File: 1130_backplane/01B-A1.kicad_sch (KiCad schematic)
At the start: 91 parts

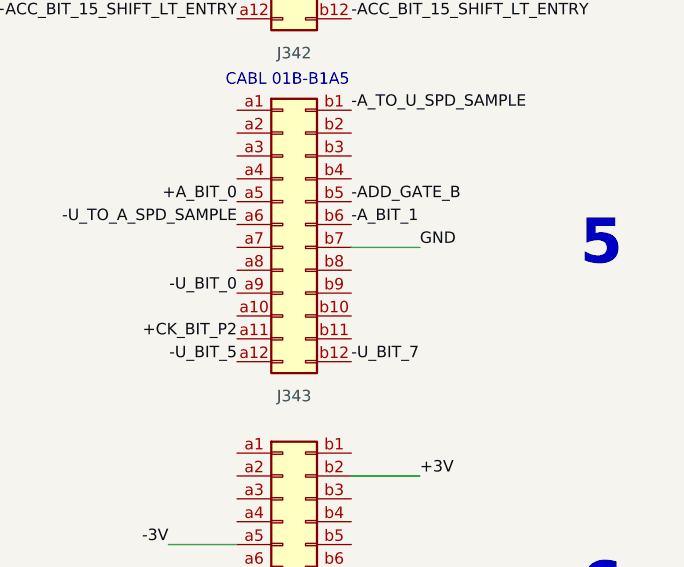
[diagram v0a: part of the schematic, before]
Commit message: Finish page RA201-RA271
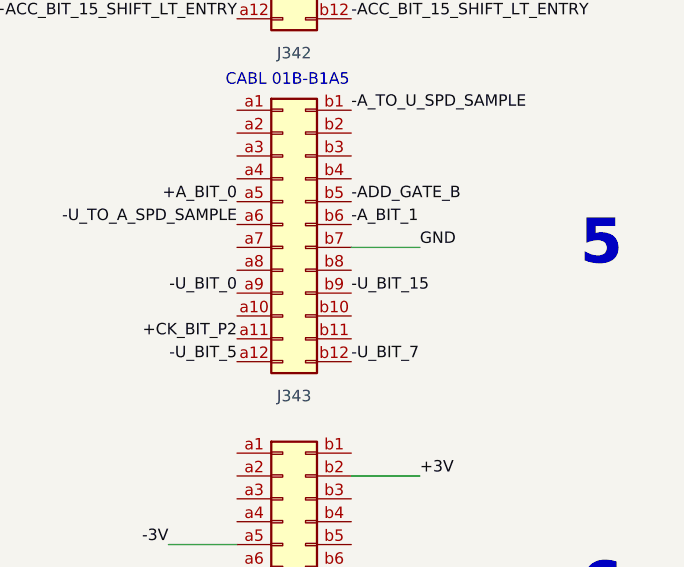
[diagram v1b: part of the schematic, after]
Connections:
- net -U_BIT_15: now also J342.b9 (Pin_b9)
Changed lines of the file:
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@@
     (effects (font (size 1.27 1.27)) (justify right bottom))
+  )
+  (label "-U_BIT_15" (at 807.72 238.76 0)
+    (effects (font (size 1.27 1.27)) (justify left bottom))
   )
   (label "-T3_SP" (at 477.52 236.22 180)

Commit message: Finish page RB101-RB171 and RB201-RB271
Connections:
- net +B_BIT_6: now also J342.a10 (Pin_a10)
- net +PHASE_B: now also J307.a1 (Pin_a1)
- net -B_BIT_0_TO_D: now also J341.a2 (Pin_a2)
- net -B_BIT_8_TO_D: now also J341.b2 (Pin_b2)
- net -RESET_D_REG_SP: now also J307.b1 (Pin_b1)
- net -RESET_D_SPD_GATE: now also J307.a3 (Pin_a3)
- net -B_BIT_2_GATED: now reaches J339.a10 (Pin_a10)
- net -B_BIT_3_GATED: now reaches J339.a11 (Pin_a11)
- net -B_BIT_4_GATED: now reaches J339.a12 (Pin_a12)
- net -B_BIT_0_GATED: now reaches J339.a8 (Pin_a8)
- net -B_BIT_1_GATED: now reaches J339.a9 (Pin_a9)
- net -B_BIT_7_GATED: now reaches J339.b10 (Pin_b10)
- net -B_BIT_5_GATED: now reaches J339.b8 (Pin_b8)
- net -B_BIT_6_GATED: now reaches J339.b9 (Pin_b9)
- net -B_BIT_8_GATED: now reaches J297.a2 (Pin_a2)
- net -B_BIT_9_GATED: now reaches J297.a3 (Pin_a3)
- net -B_BIT_10_GATED: now reaches J297.b1 (Pin_b1)
- net -B_BIT_12_GATED: now reaches J297.b3 (Pin_b3)
- net -B_BIT_13_GATED: now reaches J297.b4 (Pin_b4)
- net -B_BIT_14_GATED: now reaches J297.b5 (Pin_b5)
- net -B_BIT_15_GATED: now reaches J297.b6 (Pin_b6)
- net -B_BIT_11_GATED: now reaches J344.a8 (Pin_a8)
- net +B_BIT_7: now reaches J342.b10 (Pin_b10)
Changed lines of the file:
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@@
     (effects (font (size 1.27 1.27)) (justify left bottom))
   )
+  (label "+PHASE_B" (at 477.52 104.14 180)
+    (effects (font (size 1.27 1.27)) (justify right bottom))
+  )
   (label "-BR-2_NOT_BR-1_RESET_CCC" (at 617.22 104.14 0)
     (effects (font (size 1.27 1.27)) (justify left bottom))
@@
     (effects (font (size 1.27 1.27)) (justify right bottom))
   )
+  (label "-B_BIT_15_GATED" (at 400.05 50.8 90)
+    (effects (font (size 1.27 1.27)) (justify left bottom))
+  )
   (label "+SLC_OP" (at 172.72 279.4 0)
     (effects (font (size 1.27 1.27)) (justify left bottom))
@@
     (effects (font (size 1.27 1.27)) (justify left bottom))
   )
+  (label "-B_BIT_5_GATED" (at 807.72 121.92 0)
+    (effects (font (size 1.27 1.27)) (justify left bottom))
+  )
   (label "+STORE_STATUS_E_T2" (at 680.72 208.28 0)
     (effects (font (size 1.27 1.27)) (justify left bottom))
@@
     (effects (font (size 1.27 1.27)) (justify right bottom))
   )
+  (label "-B_BIT_6_GATED" (at 807.72 124.46 0)
+    (effects (font (size 1.27 1.27)) (justify left bottom))
+  )
   (label "+I1_POWERED" (at 426.72 167.64 0)
     (effects (font (size 1.27 1.27)) (justify left bottom))
@@
     (effects (font (size 1.27 1.27)) (justify left bottom))
   )
+  (label "-B_BIT_13_GATED" (at 394.97 50.8 90)
+    (effects (font (size 1.27 1.27)) (justify left bottom))
+  )
   (label "-START_ADVANCE" (at 160.02 185.42 180)
     (effects (font (size 1.27 1.27)) (justify right bottom))
@@
     (effects (font (size 1.27 1.27)) (justify right bottom))
   )
+  (label "-B_BIT_0_GATED" (at 795.02 121.92 180)
+    (effects (font (size 1.27 1.27)) (justify right bottom))
+  )
   (label "-T_2" (at 477.52 238.76 180)
     (effects (font (size 1.27 1.27)) (justify right bottom))
@@
     (effects (font (size 1.27 1.27)) (justify right bottom))
   )
+  (label "-B_BIT_4_GATED" (at 795.02 132.08 180)
+    (effects (font (size 1.27 1.27)) (justify right bottom))
+  )
   (label "-M_TO_I_SPD_SAMPLE" (at 617.22 114.3 0)
     (effects (font (size 1.27 1.27)) (justify left bottom))
@@
     (effects (font (size 1.27 1.27)) (justify left bottom))
   )
+  (label "-B_BIT_0_TO_D" (at 795.02 182.88 180)
+    (effects (font (size 1.27 1.27)) (justify right bottom))
+  )
   (label "-START_ADVANCE" (at 553.72 152.4 0)
     (effects (font (size 1.27 1.27)) (justify left bottom))
@@
     (effects (font (size 1.27 1.27)) (justify left bottom))
   )
+  (label "-B_BIT_14_GATED" (at 397.51 50.8 90)
+    (effects (font (size 1.27 1.27)) (justify left bottom))
+  )
   (label "-DPW_ODD_ADDR_SAR_15" (at 502.92 175.26 0)
     (effects (font (size 1.27 1.27)) (justify left bottom))
@@
     (effects (font (size 1.27 1.27)) (justify right bottom))
   )
+  (label "-B_BIT_3_GATED" (at 795.02 129.54 180)
+    (effects (font (size 1.27 1.27)) (justify right bottom))
+  )
   (label "-STORE_E" (at 223.52 144.78 180)
     (effects (font (size 1.27 1.27)) (justify right bottom))
@@
     (effects (font (size 1.27 1.27)) (justify left bottom))
   )
+  (label "-B_BIT_7_GATED" (at 807.72 127 0)
+    (effects (font (size 1.27 1.27)) (justify left bottom))
+  )
   (label "-T7_SP" (at 541.02 106.68 180)
     (effects (font (size 1.27 1.27)) (justify right bottom))
@@
     (effects (font (size 1.27 1.27)) (justify left bottom))
   )
+  (label "-B_BIT_10_GATED" (at 387.35 50.8 90)
+    (effects (font (size 1.27 1.27)) (justify left bottom))
+  )
   (label "-IX_CYCLE" (at 414.02 142.24 180)
     (effects (font (size 1.27 1.27)) (justify right bottom))
@@
     (effects (font (size 1.27 1.27)) (justify right bottom))
   )
+  (label "-RESET_D_REG_SP" (at 490.22 104.14 0)
+    (effects (font (size 1.27 1.27)) (justify left bottom))
+  )
   (label "-E_NOT_MULT_E1" (at 414.02 193.04 180)
     (effects (font (size 1.27 1.27)) (justify right bottom))
@@
     (effects (font (size 1.27 1.27)) (justify left bottom))
   )
+  (label "-B_BIT_8_GATED" (at 389.89 63.5 270)
+    (effects (font (size 1.27 1.27)) (justify right bottom))
+  )
   (label "+POWER_ON_RESET" (at 45.72 264.16 0)
     (effects (font (size 1.27 1.27)) (justify left bottom))
@@
     (effects (font (size 1.27 1.27)) (justify left bottom))
   )
+  (label "-B_BIT_2_GATED" (at 795.02 127 180)
+    (effects (font (size 1.27 1.27)) (justify right bottom))
+  )
   (label "-BR-2_NOT_BR-1_RESET_CCC" (at 160.02 276.86 180)
     (effects (font (size 1.27 1.27)) (justify right bottom))
@@
     (effects (font (size 1.27 1.27)) (justify left bottom))
   )
+  (label "-B_BIT_8_TO_D" (at 807.72 182.88 0)
+    (effects (font (size 1.27 1.27)) (justify left bottom))
+  )
   (label "-U_BIT_5" (at 172.72 294.64 0)
     (effects (font (size 1.27 1.27)) (justify left bottom))
@@
     (effects (font (size 1.27 1.27)) (justify left bottom))
   )
+  (label "-B_BIT_1_GATED" (at 795.02 124.46 180)
+    (effects (font (size 1.27 1.27)) (justify right bottom))
+  )
   (label "-T_4" (at 553.72 114.3 0)
     (effects (font (size 1.27 1.27)) (justify left bottom))
@@
     (effects (font (size 1.27 1.27)) (justify left bottom))
   )
+  (label "-RESET_D_SPD_GATE" (at 477.52 109.22 180)
+    (effects (font (size 1.27 1.27)) (justify right bottom))
+  )
   (label "+DIVIDE_OP" (at 287.02 147.32 180)
     (effects (font (size 1.27 1.27)) (justify right bottom))
@@
     (effects (font (size 1.27 1.27)) (justify left bottom))
   )
+  (label "-B_BIT_9_GATED" (at 392.43 63.5 270)
+    (effects (font (size 1.27 1.27)) (justify right bottom))
+  )
   (label "+OVERFLOW" (at 541.02 187.96 180)
     (effects (font (size 1.27 1.27)) (justify right bottom))
@@
     (effects (font (size 1.27 1.27)) (justify left bottom))
   )
+  (label "-B_BIT_11_GATED" (at 795.02 312.42 180)
+    (effects (font (size 1.27 1.27)) (justify right bottom))
+  )
   (label "-SH_RT_ROT_16_48" (at 490.22 226.06 0)
     (effects (font (size 1.27 1.27)) (justify left bottom))
@@
     (effects (font (size 1.27 1.27)) (justify left bottom))
   )
+  (label "-B_BIT_12_GATED" (at 392.43 50.8 90)
+    (effects (font (size 1.27 1.27)) (justify left bottom))
+  )
   (label "-ARITH_CTRL_B" (at 490.22 185.42 0)
     (effects (font (size 1.27 1.27)) (justify left bottom))
@@
     (effects (font (size 1.27 1.27)) (justify right bottom))
   )
+  (label "+B_BIT_6" (at 795.02 241.3 180)
+    (effects (font (size 1.27 1.27)) (justify right bottom))
+  )
   (label "KT321_AP4" (at 124.46 251.46 0)
     (effects (font (size 1.27 1.27)) (justify left bottom))
@@
     (effects (font (size 1.27 1.27)) (justify right bottom))
   )
+  (label "+B_BIT_7" (at 807.72 241.3 0)
+    (effects (font (size 1.27 1.27)) (justify left bottom))
+  )
   (label "+SINGLE_INSTR_MODE" (at 45.72 241.3 0)

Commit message: Finish page RD101-RD171
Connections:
- net +D_BIT_10: now also J342.a2 (Pin_a2)
- net +D_BIT_11: now also J342.b2 (Pin_b2)
- net +D_BIT_12: now also J342.a3 (Pin_a3)
- net +D_BIT_13: now also J342.b3 (Pin_b3)
- net +D_BIT_14: now also J342.a4 (Pin_a4)
- net +D_BIT_15: now also J342.b4 (Pin_b4)
- net RD171-AS4: now reaches J297.a4 (Pin_a4)
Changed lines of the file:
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@@
     (effects (font (size 1.27 1.27)) (justify left bottom))
   )
+  (label "+D_BIT_12" (at 795.02 223.52 180)
+    (effects (font (size 1.27 1.27)) (justify right bottom))
+  )
   (label "-STORAGE_ADDRESS_14" (at 415.29 63.5 270)
     (effects (font (size 1.27 1.27)) (justify right bottom))
@@
     (effects (font (size 1.27 1.27)) (justify right bottom))
   )
+  (label "+D_BIT_13" (at 807.72 223.52 0)
+    (effects (font (size 1.27 1.27)) (justify left bottom))
+  )
   (label "+CCC_COUNT_0" (at 299.72 167.64 0)
     (effects (font (size 1.27 1.27)) (justify left bottom))
@@
     (effects (font (size 1.27 1.27)) (justify right bottom))
   )
+  (label "+D_BIT_11" (at 807.72 220.98 0)
+    (effects (font (size 1.27 1.27)) (justify left bottom))
+  )
   (label "+PHASE_B" (at 45.72 304.8 0)
     (effects (font (size 1.27 1.27)) (justify left bottom))
@@
     (effects (font (size 1.27 1.27)) (justify left bottom))
   )
+  (label "+D_BIT_15" (at 807.72 226.06 0)
+    (effects (font (size 1.27 1.27)) (justify left bottom))
+  )
   (label "-MULTIPLY_OP" (at 223.52 106.68 180)
     (effects (font (size 1.27 1.27)) (justify right bottom))
@@
     (effects (font (size 1.27 1.27)) (justify right bottom))
   )
+  (label "RD171-AS4" (at 394.97 63.5 270)
+    (effects (font (size 1.27 1.27)) (justify right bottom))
+  )
   (label "+INTERRUPT_LVL_TGR_1" (at 426.72 294.64 0)
     (effects (font (size 1.27 1.27)) (justify left bottom))
@@
     (effects (font (size 1.27 1.27)) (justify left bottom))
   )
+  (label "+D_BIT_10" (at 795.02 220.98 180)
+    (effects (font (size 1.27 1.27)) (justify right bottom))
+  )
   (label "+XIO_E2_R_W" (at 744.22 147.32 0)
     (effects (font (size 1.27 1.27)) (justify left bottom))
@@
     (effects (font (size 1.27 1.27)) (justify right bottom))
   )
+  (label "+D_BIT_14" (at 795.02 226.06 180)
+    (effects (font (size 1.27 1.27)) (justify right bottom))
+  )

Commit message: Finish page RN101-RN111
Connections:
- net +FORMAT_5: now also J259.b1 (Pin_b1), J265.b4 (Pin_b4)
- net +MOD_8: now also J259.b5 (Pin_b5), J265.b9 (Pin_b9)
- net +MOD_9: now also J259.b6 (Pin_b6), J265.a2 (Pin_a2)
- net +OP_BIT_0: now also J259.a1 (Pin_a1), J266.b12 (Pin_b12)
- net +OP_BIT_1: now also J259.a2 (Pin_a2), J266.b8 (Pin_b8)
- net +OP_BIT_2: now also J259.a3 (Pin_a3), J266.a4 (Pin_a4)
- net +OP_BIT_3: now also J259.a4 (Pin_a4), J265.a12 (Pin_a12)
- net +OP_BIT_4: now also J259.a6 (Pin_a6), J265.a8 (Pin_a8)
- net +TAG_00: now also J265.a7 (Pin_a7)
- net +TAG_6: now also J259.b3 (Pin_b3), J266.b3 (Pin_b3)
- net +TAG_7: now also J259.b4 (Pin_b4), J265.a11 (Pin_a11)
- net -ADD_TO_STOR_INTLK: now also J266.b11 (Pin_b11)
- net -B_BIT_0_GATED: now also J266.b9 (Pin_b9)
- net -B_BIT_1_GATED: now also J266.a8 (Pin_a8)
- net -B_BIT_2_GATED: now also J266.b1 (Pin_b1)
- net -B_BIT_3_GATED: now also J265.b12 (Pin_b12)
- net -B_BIT_4_GATED: now also J265.b5 (Pin_b5)
- net -B_BIT_5_GATED: now also J265.a4 (Pin_a4)
- net -B_BIT_6_GATED: now also J266.a2 (Pin_a2)
- net -B_BIT_7_GATED: now also J265.b11 (Pin_b11)
- net -B_BIT_8_GATED: now also J265.a3 (Pin_a3)
- net -B_BIT_9_GATED: now also J265.b3 (Pin_b3)
- net -DC_RESET_OP_REG_AND_OP_FLAGS: now also J266.a9 (Pin_a9)
- net -DPW_ODD_ADDR_SET_GT: now also J266.a7 (Pin_a7)
- net -FORMAT_5: now also J265.a1 (Pin_a1)
- net -MOD_8: now also J265.b6 (Pin_b6), J340.a8 (Pin_a8)
- net -MOD_9: now also J265.b1 (Pin_b1)
- net -NOT_END_OP_TO_SP: now also J266.a6 (Pin_a6), J266.b6 (Pin_b6)
- net -OP_BIT_0: now also J266.b10 (Pin_b10)
- net -OP_BIT_1: now also J266.b5 (Pin_b5)
- net -OP_BIT_2: now also J266.a1 (Pin_a1)
- net -OP_BIT_3: now also J265.a9 (Pin_a9)
- net -OP_BIT_4: now also J265.a6 (Pin_a6)
- net -TAG_00: now also J265.b8 (Pin_b8)
- net -TAG_6: now also J266.b4 (Pin_b4)
- net -TAG_7: now also J265.b10 (Pin_b10)
- net -DBL_WORD_ADD_ADDR: now reaches J266.a11 (Pin_a11)
- net -DBL_WORD_ADD_ADDR: now also J344.b6 (Pin_b6)
- net RN111_AD4: now reaches J266.a12 (Pin_a12)
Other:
- note added: "5804646"

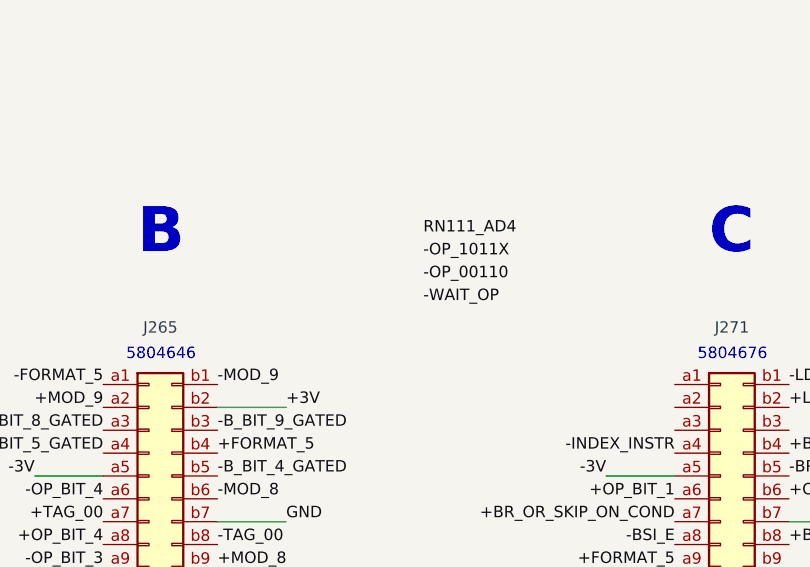
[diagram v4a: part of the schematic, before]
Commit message: Finish page RN101-RN111, forgot DOT OR
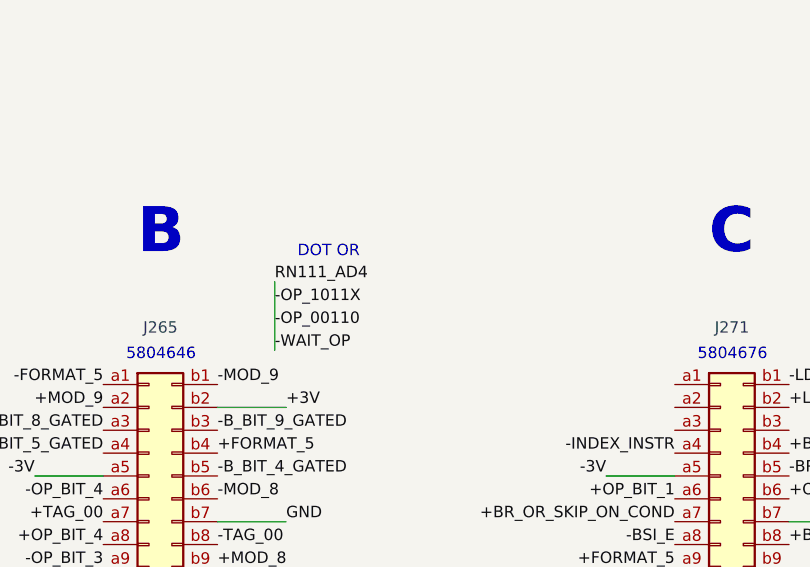
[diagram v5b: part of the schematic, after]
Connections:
- net -OP_1011X is gone; now on net -OP_00110: J277.b1 (Pin_b1)
- net -WAIT_OP is gone; now on net -OP_00110: J284.b6 (Pin_b6), J287.a7 (Pin_a7), J293.b4 (Pin_b4), J336.a4 (Pin_a4)
- net RN111_AD4 is gone; now on net -OP_00110: J266.a12 (Pin_a12)
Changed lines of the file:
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@@
     (stroke (width 0) (type default) (color 0 0 0 0))
   )
+  (wire (pts (xy 115.57 92.71) (xy 115.57 100.33))
+    (stroke (width 0) (type default) (color 0 0 0 0))
+  )
   (polyline (pts (xy 30.48 43.18) (xy 30.48 41.91))
     (stroke (width 0) (type solid) (color 0 0 0 0))
@@
     (effects (font (size 1.27 1.27)) (justify left bottom))
   )
+  (text "DOT OR" (at 118.11 90.17 0)
+    (effects (font (size 1.27 1.27)) (justify left bottom))
+  )
   (text "A" (at 331.47 368.3 0)
     (effects (font (size 1.27 1.27)) (justify left bottom))
@@
     (effects (font (size 1.27 1.27)) (justify left bottom))
   )
-  (label "RN111_AD4" (at 132.08 87.63 0)
+  (label "RN111_AD4" (at 115.57 92.71 0)
     (effects (font (size 1.27 1.27)) (justify left bottom))
   )
@@
     (effects (font (size 1.27 1.27)) (justify right bottom))
   )
-  (label "-OP_00110" (at 132.08 92.71 0)
+  (label "-OP_00110" (at 115.57 97.79 0)
     (effects (font (size 1.27 1.27)) (justify left bottom))
   )
@@
     (effects (font (size 1.27 1.27)) (justify left bottom))
   )
-  (label "-OP_1011X" (at 132.08 90.17 0)
+  (label "-OP_1011X" (at 115.57 95.25 0)
     (effects (font (size 1.27 1.27)) (justify left bottom))
   )
@@
     (effects (font (size 1.27 1.27)) (justify right bottom))
   )
-  (label "-WAIT_OP" (at 132.08 95.25 0)
+  (label "-WAIT_OP" (at 115.57 100.33 0)
     (effects (font (size 1.27 1.27)) (justify left bottom))
   )

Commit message: Finish page RQ101-RQ171
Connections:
- net +Q_BIT_0: now also J342.a7 (Pin_a7)
- net +Q_BIT_14: now also J342.a8 (Pin_a8)
- net +Q_BIT_15: now also J342.b8 (Pin_b8)
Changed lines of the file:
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@@
     (effects (font (size 1.27 1.27)) (justify right bottom))
+  )
+  (label "+Q_BIT_15" (at 807.72 236.22 0)
+    (effects (font (size 1.27 1.27)) (justify left bottom))
   )
   (label "KM201_AQ4" (at 477.52 269.24 180)
@@
     (effects (font (size 1.27 1.27)) (justify left bottom))
   )
+  (label "+Q_BIT_0" (at 795.02 233.68 180)
+    (effects (font (size 1.27 1.27)) (justify right bottom))
+  )
   (label "-B_BIT_0_LATCHED" (at 477.52 180.34 180)
     (effects (font (size 1.27 1.27)) (justify right bottom))
@@
     (effects (font (size 1.27 1.27)) (justify right bottom))
   )
+  (label "+Q_BIT_14" (at 795.02 236.22 180)
+    (effects (font (size 1.27 1.27)) (justify right bottom))
+  )

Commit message: Finish page RS101-RS121, Processor logic finished! Now for I/O and Memory.
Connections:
- net +CCC_1: now also J259.a7 (Pin_a7), J292.b11 (Pin_b11)
- net +CCC_16: now also J259.b9 (Pin_b9), J291.a6 (Pin_a6)
- net +CCC_COUNT_0: now also J291.a2 (Pin_a2)
- net +CCC_COUNT_0_OR_1: now also J291.b1 (Pin_b1)
- net +MOD_8: now also J291.b11 (Pin_b11)
- net +MOD_9: now also J291.a9 (Pin_a9)
- net +SHIFT_CTRL: now also J292.b9 (Pin_b9)
- net +SHIFT_RIGHT_OP: now also J291.b8 (Pin_b8)
- net +SH_RT_ROT_16_48: now also J291.b10 (Pin_b10)
- net -B_BIT_10_GATED: now also J291.b5 (Pin_b5)
- net -B_BIT_11_GATED: now also J291.b4 (Pin_b4)
- net -B_BIT_12_GATED: now also J291.b12 (Pin_b12)
- net -B_BIT_13_GATED: now also J292.a3 (Pin_a3)
- net -B_BIT_14_GATED: now also J292.b8 (Pin_b8)
- net -B_BIT_15_GATED: now also J292.a9 (Pin_a9)
- net -CARRY_TO_ACC: now also J292.b3 (Pin_b3)
- net -CCC_16_TO_ACC: now also J291.a4 (Pin_a4)
- net -CCC_1_TO_ACC: now also J292.a8 (Pin_a8)
- net -CCC_32_TO_ACC: now also J291.a3 (Pin_a3)
- net -CCC_4_TO_ACC: now also J292.b12 (Pin_b12)
- net -CCC_8_TO_ACC: now also J292.a2 (Pin_a2)
- net -CCC_COUNT_0: now also J291.b3 (Pin_b3)
- net -CCC_COUNT_0_OR_1: now also J291.a1 (Pin_a1)
- net -CCC_DECREM_SAMPLE: now also J292.a6 (Pin_a6)
- net -DC_RESET_CCC: now also J292.a1 (Pin_a1)
- net -EXCHG_A_AND_Q_SPD_SAMPLE: now also J291.a8 (Pin_a8)
- net -E_CYCLES: now also J292.b6 (Pin_b6)
- net -GATE_CCC_TO_A10-A15: now also J292.b4 (Pin_b4)
- net -SET_CCC_1: now also J292.a7 (Pin_a7)
- net -SET_CCC_16: now also J291.a7 (Pin_a7)
- net -SET_CCC_18: now also J292.b5 (Pin_b5)
- net -SH_RT_ROT_16_48: now also J292.b1 (Pin_b1)
- net -T3_SP: now also J292.b10 (Pin_b10)
- net GND: now also J292.a11 (Pin_a11)
- net +CCC_4: now reaches J292.a12 (Pin_a12)
- net +CCC_4: now also J259.a9 (Pin_a9)
- net +CCC_2: now reaches J292.a4 (Pin_a4)
- net +CCC_2: now also J259.a8 (Pin_a8)
- net +CCC_8: now reaches J291.a12 (Pin_a12)
- net +CCC_8: now also J259.b8 (Pin_b8)
- net +CCC_32: now reaches J291.b6 (Pin_b6)
- net +CCC_32: now also J259.b10 (Pin_b10)
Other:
- note added: "5804608"

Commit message: Finish page WZ051 and WZ061
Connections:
- net -SENSE_AMP_BIT_16: now also J297.a9 (Pin_a9)
- net -SENSE_AMP_BIT_17: now also J344.a12 (Pin_a12)
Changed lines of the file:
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@@
     (effects (font (size 1.27 1.27)) (justify left bottom))
+  )
+  (label "-SENSE_AMP_BIT_17" (at 795.02 322.58 180)
+    (effects (font (size 1.27 1.27)) (justify right bottom))
   )
   (label "-A_TO_U_SPD_SAMPLE" (at 731.52 243.84 180)
@@
     (effects (font (size 1.27 1.27)) (justify left bottom))
   )
+  (label "-SENSE_AMP_BIT_16" (at 407.67 63.5 270)
+    (effects (font (size 1.27 1.27)) (justify right bottom))
+  )
   (label "+T6_PWR_1" (at 477.52 274.32 180)
